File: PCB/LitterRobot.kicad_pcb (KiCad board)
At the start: 4 copper layers, 55 x 140 mm, 150 parts, among them J1 DF11C-4DP-2V(57), J2 DF11C-6DP-2V(57), J3 DF11C-8DP-2V(57), J4 DF11C-6DP-2V(57), J5 TSM-105-01-S-DV, Q1 BSS138, Q10 BC817, Q11 BC817, Q12 BC817, Q13 BC817, Q14 BC817, Q15 BC817, Q16 BC817, Q17 BC817, Q18 BC817, Q19 BC817, Q2 BSS138, Q20 BC817, Q21 BC817, Q22 BC817, Q23 BC817, Q24 BC817, Q3 BC817, Q4 BC817, Q5 BC817, Q6 BC817, Q7 BC817, Q8 BC817, Q9 BC817, SW1 PCB_Push_Button, SW2 PCB_Push_Button, SW3 PCB_Push_Button, SW4 PCB_Push_Button, SW5 PCB_Push_Button, SW6 PCB_Push_Button, U1 MPM54304GMN-0001, U2 10CL016YE144C8G, U3 S25FL128SAGMFI000, U4 DRV8871DDA, U5 MCP1700T-5002E/TT, U6 VEML6035, X1 X1G0044510011

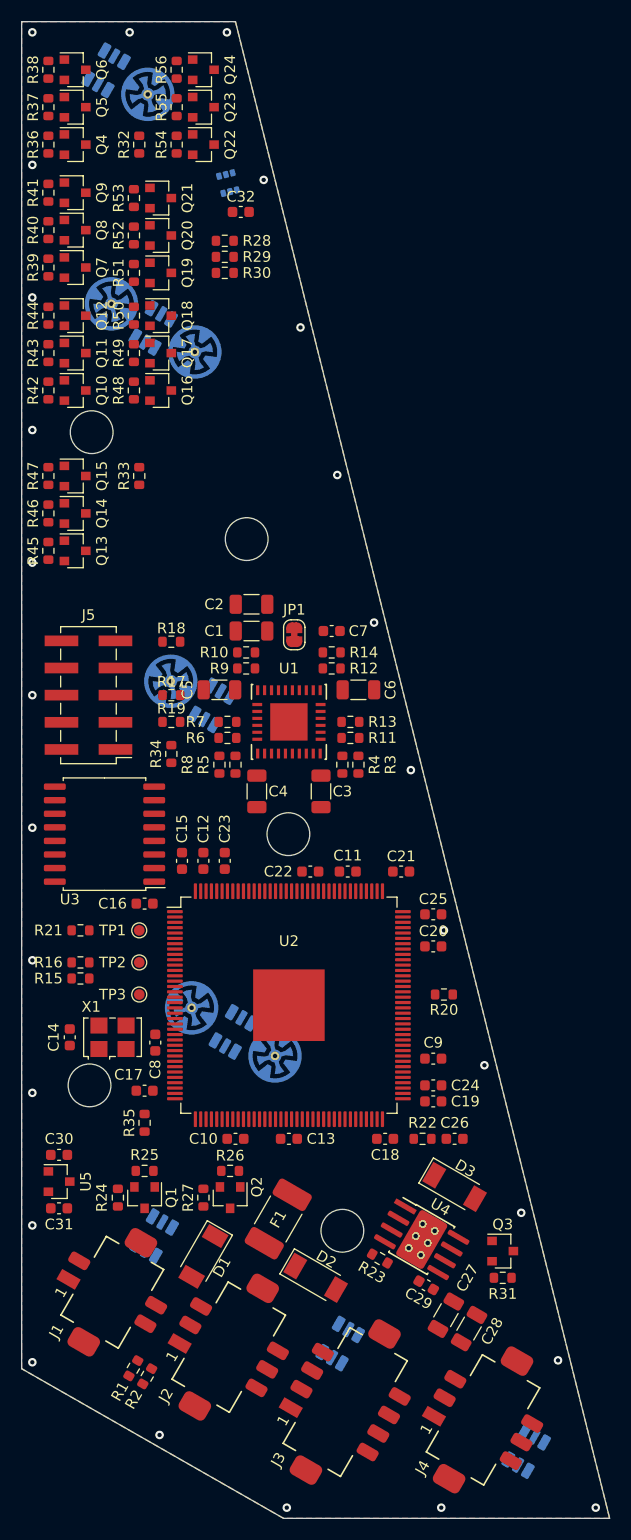
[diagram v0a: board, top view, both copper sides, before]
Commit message: Place the Bluetooth module on the PCB
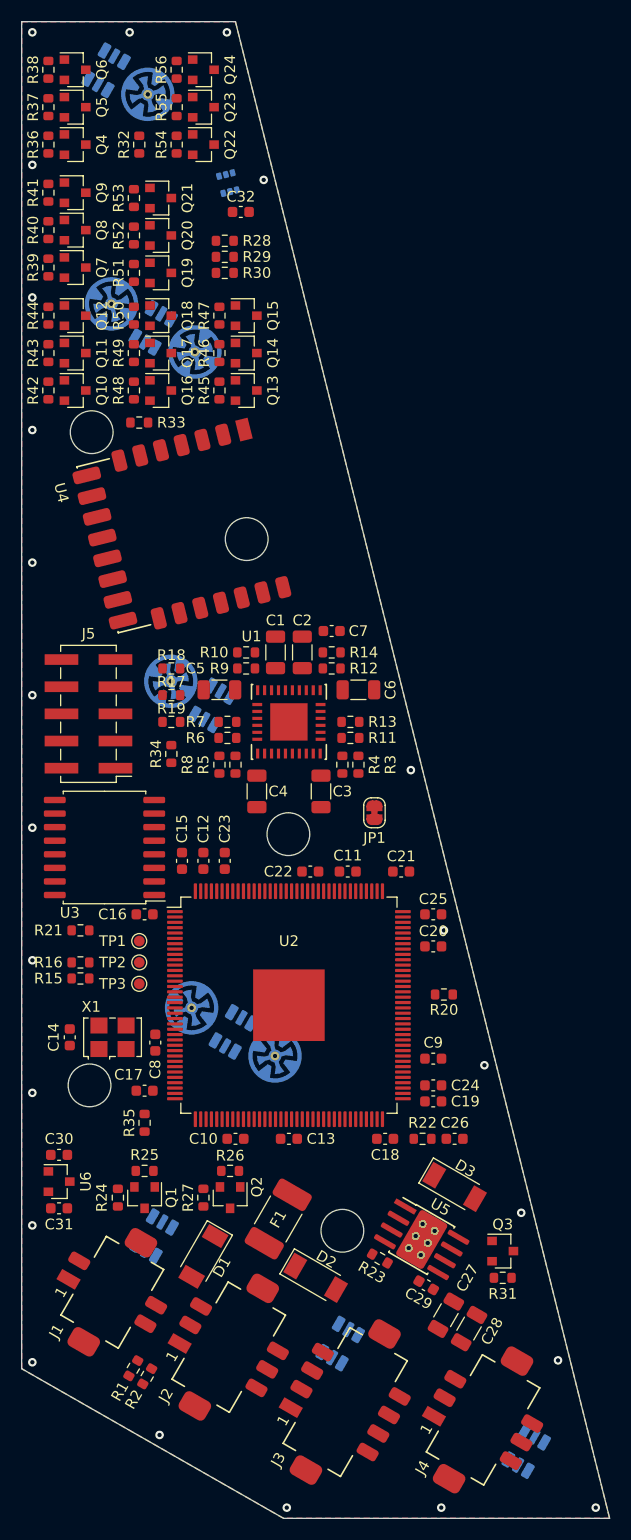
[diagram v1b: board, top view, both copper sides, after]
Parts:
- added U4: EMB1061, LitterRobot:MXCHIP_EMB1061, F.Cu at (85.8, 81.5)
- moved Q13 21.9 mm to (88.0, 69.5)
- moved Q14 21.9 mm to (88.0, 66.0)
- moved Q15 21.9 mm to (88.0, 62.5)
- moved R45 21.9 mm to (85.5, 69.5)
- moved R46 21.9 mm to (85.5, 66.0)
- moved R47 21.9 mm to (85.5, 62.5)
- moved JP1 18.3 mm to (100.0, 109.0), turned to 270 degrees
- moved C2 6.54 mm to (93.2, 94.0), turned to 90 degrees
- moved R33 5.00 mm to (78.0, 72.5), turned to 180 degrees
- moved C1 3.01 mm to (90.8, 94.0), turned to 90 degrees
- moved R18 2.50 mm to (81.0, 95.5)
- moved J5 1.75 mm to (73.2, 99.8)
- moved U3 1.25 mm to (74.8, 112.2)
- moved C16 1.00 mm to (78.5, 118.5)
- moved TP1 1.00 mm to (78.0, 121.0)
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- renumbered U4 to U5, U5 to U6, U6 to U7
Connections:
- U2 pad 100: (no net) -> /Bluetooth/Bluetooth_RX
- U2 pad 101: (no net) -> /Bluetooth/Bluetooth_~RTS
- U2 pad 103: (no net) -> /Bluetooth/Bluetooth_~CTS
- U2 pad 98: (no net) -> /Bluetooth/Bluetooth_~RESET
- U2 pad 99: (no net) -> /Bluetooth/Bluetooth_TX
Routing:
- net GND: vias 26 -> 23

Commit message: Start routing the PCB
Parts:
- moved R26 3.54 mm to (84.0, 145.0), turned to 270 degrees
- moved R27 3.54 mm to (86.5, 142.5), turned to 180 degrees
- moved R21 3.00 mm to (72.5, 123.0)
- moved R16 2.00 mm to (72.5, 121.0)
- moved C1 0.50 mm to (90.8, 93.5)
- moved C2 0.50 mm to (93.2, 93.5)
- moved R15 0.50 mm to (72.5, 125.0)
- moved TP1 0.50 mm to (78.0, 120.5)
- moved TP2 0.25 mm to (78.0, 122.8)
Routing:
- net +7V: track 0.00 -> 326.5 mm, vias 0 -> 10
- net +1V2: track 0.00 -> 186.3 mm, vias 0 -> 15
- net +15V: track 0.00 -> 152.3 mm, vias 0 -> 9
- net +2V5: track 0.00 -> 121.6 mm, vias 0 -> 5
- net +3V3: track 0.00 -> 58.3 mm, vias 0 -> 16
- net GND: track 0.00 -> 24.1 mm, vias 23 -> 74
- net /Cycle_button: track 0.00 -> 23.6 mm
- net /FPGA/FPGA config/DCLK: track 0.00 -> 22.4 mm
- net /FPGA/FPGA config/~CS: track 0.00 -> 19.7 mm
- net Net-(R21-Pad2): track 0.00 -> 19.2 mm
- net /Hall_sensor_VCC: track 0.00 -> 17.4 mm
- net /FPGA/FPGA config/ASDO: track 0.00 -> 13.4 mm, vias 0 -> 2
- net /DFI_2: track 0.00 -> 11.6 mm
- net /FPGA/FPGA config/DATA0: track 0.00 -> 10.4 mm
- net /FPGA/Power_good: track 0.00 -> 9.69 mm
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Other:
- net class Default: trace_width 0.25 -> 0.2

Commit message: Improve the PCB push button footprints
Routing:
- net /Reset_button: track 0.00 -> 24.0 mm
- net +7V: track 326.5 -> 330.3 mm
- net +3V3: track 58.3 -> 60.7 mm, vias 16 -> 18

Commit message: Route more signals
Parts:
- moved Q16 30.3 mm to (84.0, 39.5)
- moved Q24 30.3 mm to (80.0, 69.5)
- moved R48 30.3 mm to (81.5, 39.5)
- moved R56 30.3 mm to (77.5, 69.5)
- moved Q17 23.3 mm to (84.0, 43.0)
- moved Q23 23.3 mm to (80.0, 66.0)
- moved R49 23.3 mm to (81.5, 43.0)
- moved R55 23.3 mm to (77.5, 66.0)
- moved Q10 18.5 mm to (72.0, 51.0)
- moved R42 18.5 mm to (69.5, 51.0)
- moved Q18 16.5 mm to (84.0, 46.5)
- moved Q22 16.5 mm to (80.0, 62.5)
- moved R50 16.5 mm to (81.5, 46.5)
- moved R54 16.5 mm to (77.5, 62.5)
- moved D3 12.2 mm to (101.4, 154.6)
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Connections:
- U2 pad 100: /Bluetooth/Bluetooth_RX -> /Bluetooth/Bluetooth_~RTS
- U2 pad 101: /Bluetooth/Bluetooth_~RTS -> /Bluetooth/Bluetooth_~CTS
- U2 pad 103: /Bluetooth/Bluetooth_~CTS -> /Bluetooth/Bluetooth_RX
- U2 pad 112: /FPGA/Light_sensor_SCL -> /FPGA/Light_sensor_INT
- U2 pad 113: /FPGA/Light_sensor_INT -> /FPGA/Light_sensor_SCL
- U2 pad 136: /FPGA/Hall_sensor_L -> /DFI_1
- U2 pad 137: /FPGA/Hall_sensor_R -> /DFI_2
- U2 pad 141: /Extension_1 -> /Extension_4
- U2 pad 142: /Extension_2 -> /Extension_1
- U2 pad 144: /Extension_4 -> /Extension_2
- U2 pad 44: /FPGA/Motor_PWM_1 -> /FPGA/Hall_sensor_R
- U2 pad 46: /FPGA/Motor_PWM_2 -> /FPGA/Hall_sensor_L
- U2 pad 58: /Dome LED/Dome_LED -> (no net)
- U2 pad 59: /DFI_1 -> /FPGA/Motor_PWM_1
- U2 pad 60: /DFI_2 -> /FPGA/Motor_PWM_2
- U2 pad 66: /FPGA/Weight_ref -> /Weight_sensor_P
- U2 pad 67: /Weight_sensor_P -> /Weight_sensor_N
- U2 pad 68: /Weight_sensor_N -> /FPGA/Weight_ref
- U2 pad 83: (no net) -> /Dome LED/Dome_LED
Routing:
- net +3V3: track 60.7 -> 342.0 mm, vias 18 -> 21
- net Net-(D9-Pad4): track 1.00 -> 144.7 mm, vias 1 -> 2
- net Net-(D9-Pad5): track 1.00 -> 138.2 mm, vias 1 -> 2
- net Net-(D9-Pad6): track 1.00 -> 133.8 mm, vias 1 -> 2
- net /Power_button: track 4.21 -> 112.1 mm, vias 0 -> 1
- net Net-(D10-Pad4): track 1.00 -> 106.5 mm, vias 1 -> 2
- net Net-(D10-Pad5): track 1.00 -> 98.4 mm, vias 1 -> 2
- net Net-(D10-Pad6): track 1.00 -> 91.0 mm, vias 1 -> 2
- net /FPGA/Light_sensor_SCL: track 0.00 -> 86.7 mm, vias 0 -> 2
- net /FPGA/Light_sensor_SDA: track 0.00 -> 85.3 mm, vias 0 -> 2
- net /FPGA/Light_sensor_INT: track 0.00 -> 84.9 mm, vias 0 -> 2
- net /Bluetooth/Bluetooth_~RESET: track 2.20 -> 85.8 mm, vias 1 -> 2
- net /Cycle_button: track 23.6 -> 106.3 mm, vias 0 -> 1
- net /Bluetooth/Bluetooth_~RTS: track 0.00 -> 77.6 mm, vias 0 -> 2
- net /Extension_1: track 0.00 -> 76.9 mm, vias 0 -> 2
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- added copper zone on In1.Cu, net GND
- removed copper zone on In1.Cu, net +3V3

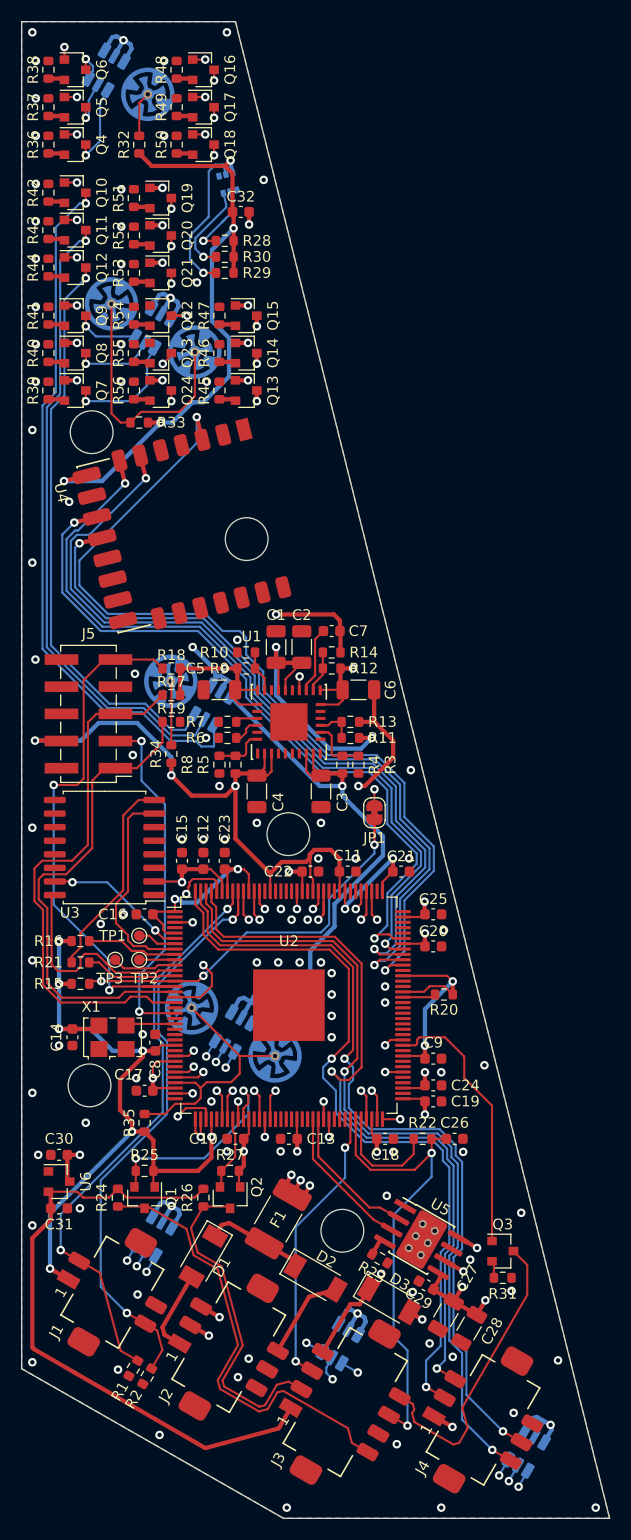
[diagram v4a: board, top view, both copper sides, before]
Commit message: Complete routing all signals
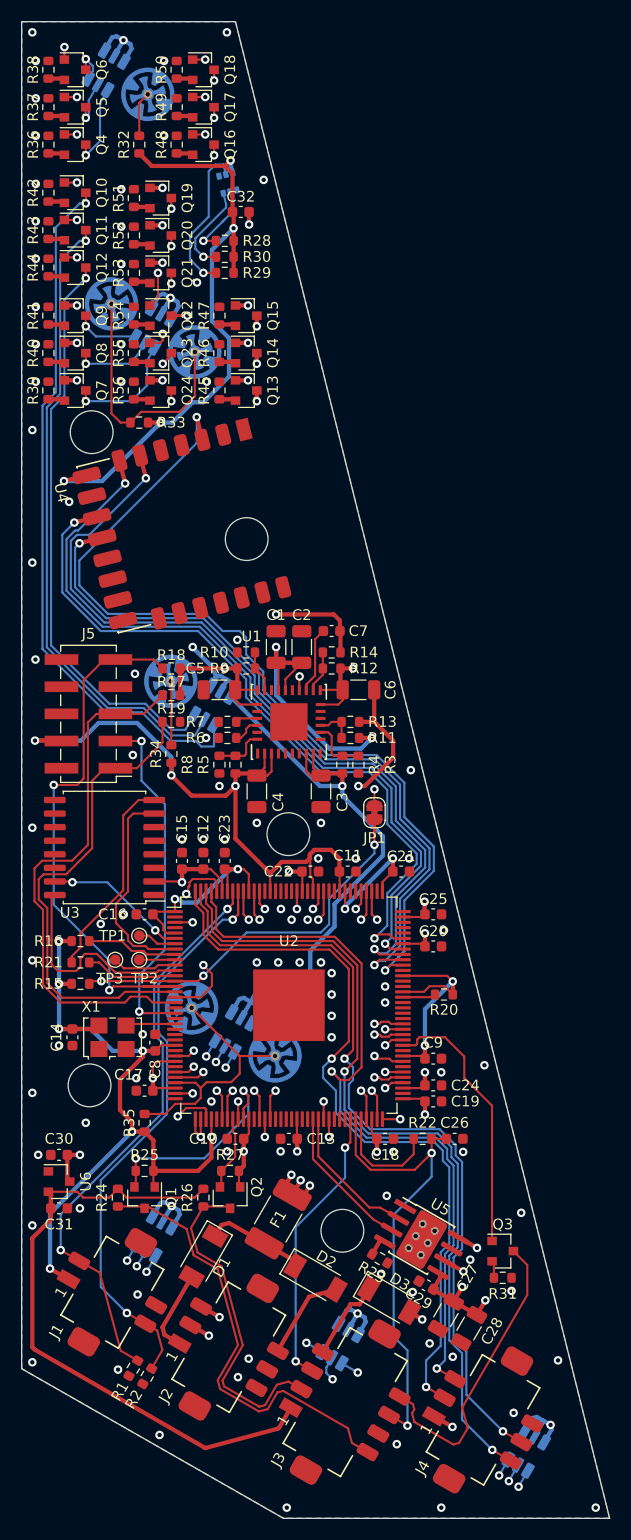
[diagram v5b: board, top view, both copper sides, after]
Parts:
- moved Q16 7.00 mm to (84.0, 46.5)
- moved Q18 7.00 mm to (84.0, 39.5)
- moved R48 7.00 mm to (81.5, 46.5)
- moved R50 7.00 mm to (81.5, 39.5)
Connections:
- Q5 pad 1: /FPGA/Power_LED_B -> /Control panel/Power_LED_R
- U2 pad 120: /Control panel/Cycle_LED_R -> /Control panel/Reset_LED_G
- U2 pad 121: /Control panel/Cycle_LED_G -> /Control panel/Reset_LED_R
- U2 pad 125: /Control panel/Cycle_LED_B -> /Control panel/Reset_LED_B
- U2 pad 132: /Control panel/Power_LED_B -> /Control panel/Left_LED_G
- U2 pad 133: /Control panel/Power_LED_G -> /Control panel/Left_LED_R
- U2 pad 135: /FPGA/Power_LED_B -> /Control panel/Left_LED_B
- U2 pad 39: /Control panel/Right_LED_R -> /Control panel/Cycle_LED_R
- U2 pad 42: /Control panel/Right_LED_G -> /Control panel/Cycle_LED_B
- U2 pad 43: /Control panel/Right_LED_B -> /Control panel/Cycle_LED_G
- U2 pad 49: /Control panel/Center_LED_R -> /Control panel/Empty_LED_B
- U2 pad 50: /Control panel/Center_LED_G -> /Control panel/Empty_LED_R
- U2 pad 51: /Control panel/Center_LED_B -> /Control panel/Empty_LED_G
- U2 pad 69: /Control panel/Left_LED_R -> /Control panel/Right_LED_G
- U2 pad 71: /Control panel/Left_LED_G -> /Control panel/Power_LED_B
- U2 pad 72: /Control panel/Left_LED_B -> /Control panel/Power_LED_G
- U2 pad 76: /Control panel/Reset_LED_R -> /Control panel/Power_LED_R
- U2 pad 77: /Control panel/Reset_LED_G -> /Control panel/Right_LED_R
- U2 pad 80: /Control panel/Reset_LED_B -> /Control panel/Right_LED_B
- U2 pad 85: /Control panel/Empty_LED_R -> /Control panel/Center_LED_B
- U2 pad 86: /Control panel/Empty_LED_G -> /Control panel/Center_LED_G
- U2 pad 87: /Control panel/Empty_LED_B -> /Control panel/Center_LED_R
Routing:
- net Net-(D8-Pad4): track 2.73 -> 198.9 mm
- net Net-(D8-Pad5): track 2.73 -> 193.4 mm
- net Net-(D8-Pad6): track 2.73 -> 185.8 mm
- net Net-(D7-Pad6): track 2.73 -> 133.7 mm
- net Net-(D7-Pad5): track 2.73 -> 129.4 mm
- net /Control panel/Power_LED_B: track 3.04 -> 126.2 mm
- net Net-(D7-Pad4): track 2.73 -> 123.8 mm
- net /Control panel/Power_LED_R: track 0.00 -> 120.3 mm, vias 0 -> 2
- net /Control panel/Power_LED_G: track 4.04 -> 119.3 mm
- net /Control panel/Center_LED_G: track 2.84 -> 103.6 mm
- net /Control panel/Empty_LED_G: track 1.17 -> 101.8 mm, vias 1 -> 2
- net /Control panel/Empty_LED_R: track 1.17 -> 101.6 mm, vias 1 -> 2
- net /Control panel/Right_LED_G: track 2.87 -> 101.8 mm, vias 1 -> 2
- net /Control panel/Center_LED_R: track 4.04 -> 101.1 mm
- net /Control panel/Left_LED_B: track 2.84 -> 96.7 mm
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
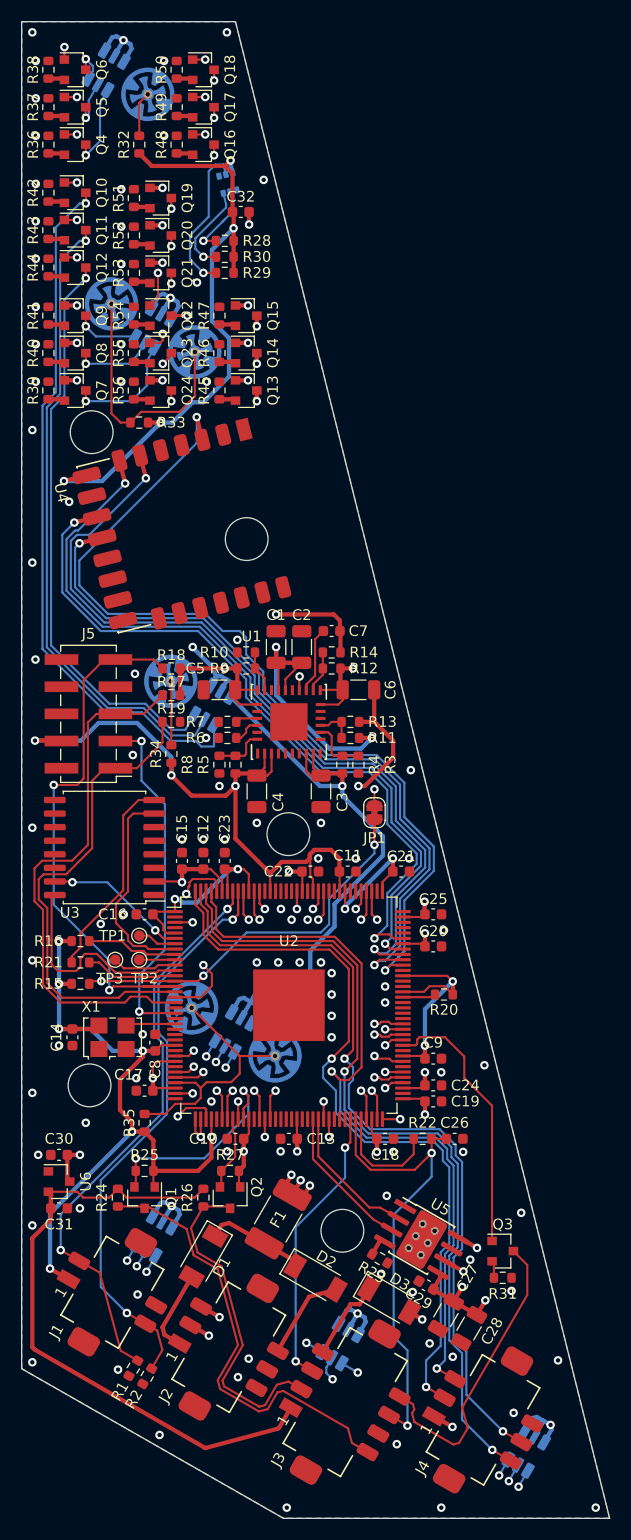
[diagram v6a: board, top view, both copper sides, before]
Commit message: Add jumpers on the power supply outputs
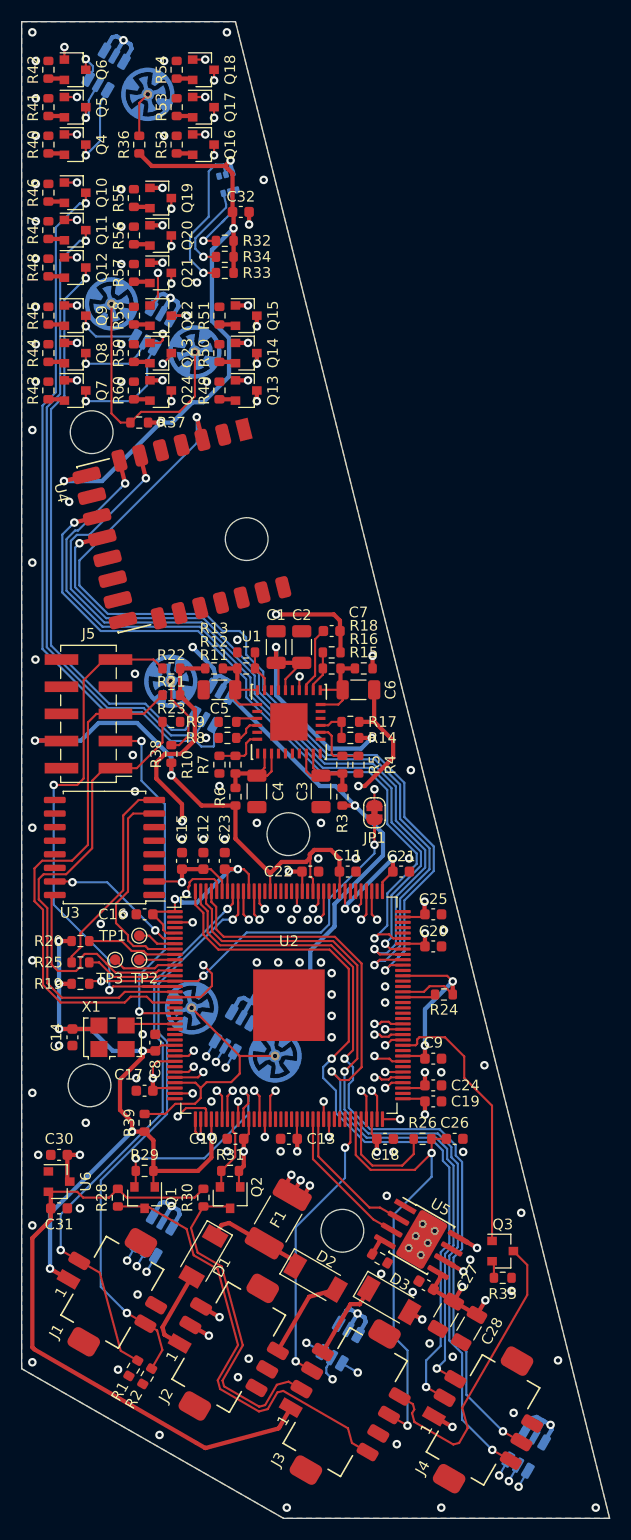
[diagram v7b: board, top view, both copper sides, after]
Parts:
- added R11: 0R, Resistor_SMD:R_0603_1608Metric, F.Cu at (85.0, 95.5)
- added R15: 0R, Resistor_SMD:R_0603_1608Metric, F.Cu at (99.0, 95.5)
- added R3: 0R, Resistor_SMD:R_0603_1608Metric, F.Cu at (97.0, 107.5)
- added R6: 0R, Resistor_SMD:R_0603_1608Metric, F.Cu at (87.0, 107.5)
- renumbered R8 to R10, R9 to R12, R10 to R13, R11 to R14, R12 to R16, R13 to R17, R14 to R18, R15 to R19, R16 to R20, R17 to R21, R18 to R22, R19 to R23, R20 to R24, R21 to R25, R22 to R26, R23 to R27, R24 to R28, R25 to R29, R26 to R30, R27 to R31, R28 to R32, R29 to R33, R30 to R34, R31 to R35, R32 to R36, R33 to R37, R34 to R38, R35 to R39, R3 to R4, R36 to R40, R37 to R41, R38 to R42, R39 to R43, R40 to R44, R41 to R45, R42 to R46, R43 to R47, R44 to R48, R45 to R49, R4 to R5, R46 to R50, R47 to R51, R48 to R52, R49 to R53, R50 to R54, R51 to R55, R52 to R56, R53 to R57, R54 to R58, R55 to R59, R56 to R60, R5 to R7, R6 to R8, R7 to R9
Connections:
- C3 pad 1: +7V -> Net-(C3-Pad1)
- C4 pad 1: +3V3 -> Net-(C4-Pad1)
- C5 pad 1: +2V5 -> Net-(C5-Pad1)
- C6 pad 1: +1V2 -> Net-(C6-Pad1)
- R12 pad 1: +2V5 -> Net-(C5-Pad1)
- R16 pad 1: +1V2 -> Net-(C6-Pad1)
- R4 pad 1: +7V -> Net-(C3-Pad1)
- R7 pad 1: +3V3 -> Net-(C4-Pad1)
- U1 pad 1: +2V5 -> Net-(C5-Pad1)
- U1 pad 14: +7V -> Net-(C3-Pad1)
- U1 pad 15: +7V -> Net-(C3-Pad1)
- U1 pad 22: +1V2 -> Net-(C6-Pad1)
- U1 pad 23: +1V2 -> Net-(C6-Pad1)
- U1 pad 32: +2V5 -> Net-(C5-Pad1)
- U1 pad 8: +3V3 -> Net-(C4-Pad1)
- U1 pad 9: +3V3 -> Net-(C4-Pad1)
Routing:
- net +3V3: track 342.0 -> 331.3 mm, vias 21 -> 20
- net Net-(C4-Pad1): track 0.00 -> 8.82 mm
- net Net-(C3-Pad1): track 0.00 -> 8.82 mm
- net Net-(C5-Pad1): track 0.00 -> 8.75 mm
- net Net-(C6-Pad1): track 0.00 -> 8.58 mm
- net +7V: track 300.4 -> 292.3 mm
- net +2V5: track 114.3 -> 106.6 mm
- net +1V2: track 193.1 -> 188.1 mm
- net /Empty_button: track 62.1 -> 63.8 mm
- net GND: vias 96 -> 97
